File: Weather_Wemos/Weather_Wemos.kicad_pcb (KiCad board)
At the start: 2 copper layers, 62 x 85 mm, 23 parts, among them J1 Pwr In, J2 12V, J3 Rain3 Adv, J4 WIND, J5 RAIN1, J6 Rain2 Serial, J7 Exp, U1 WeMos_D1_mini, U2 L7805

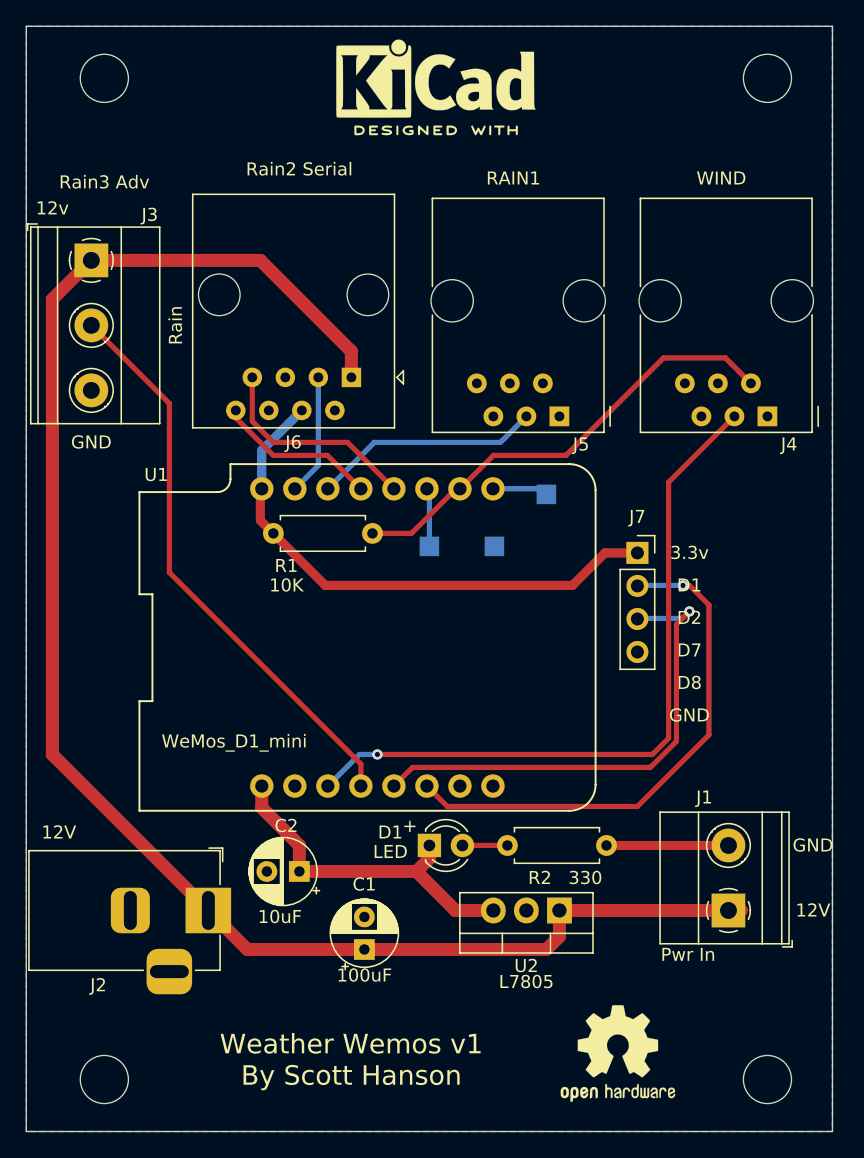
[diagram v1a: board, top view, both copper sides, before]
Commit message: upgraded to 6, changed pinout
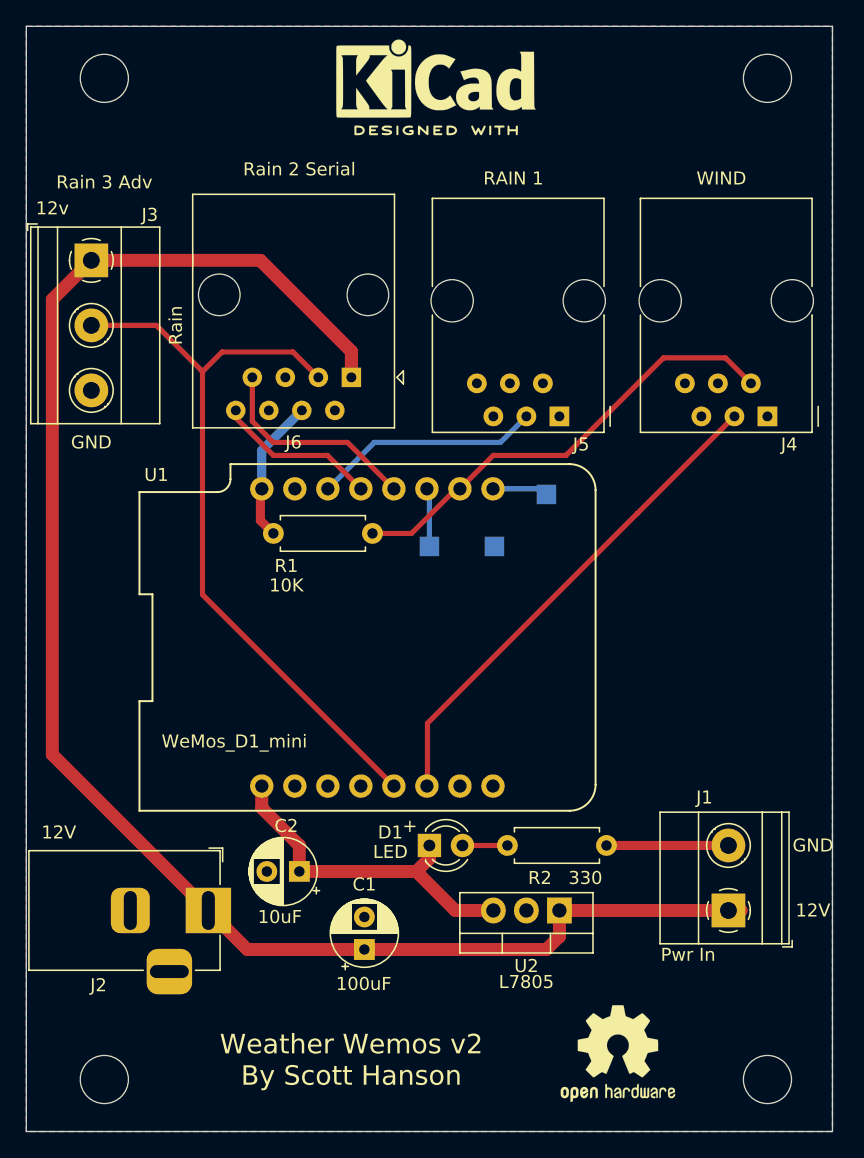
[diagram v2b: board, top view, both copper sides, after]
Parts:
- removed J7: Exp, Connector_PinSocket_2.54mm:PinSocket_1x04_P2.54mm_Vertical
- J3: value Rain3 Adv -> Rain 3 Adv
- J5: value RAIN1 -> RAIN 1
- J6: value Rain2 Serial -> Rain 2 Serial
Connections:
- J3 pad 2: RAIN3 -> RAIN2
- J4 pad 1: Net-(J4-Pad1) -> unconnected-(J4-Pad1)
- J4 pad 6: Net-(J4-Pad6) -> unconnected-(J4-Pad6)
- J5 pad 1: Net-(J5-Pad1) -> unconnected-(J5-Pad1)
- J5 pad 2: Net-(J5-Pad2) -> unconnected-(J5-Pad2)
- J5 pad 5: Net-(J5-Pad5) -> unconnected-(J5-Pad5)
- J5 pad 6: Net-(J5-Pad6) -> unconnected-(J5-Pad6)
- U1 pad 11: WSPEED -> unconnected-(U1-Pad11)
- U1 pad 12: RAIN3 -> unconnected-(U1-Pad12)
- U1 pad 13: D2 -> RAIN2
- U1 pad 14: D1 -> WSPEED
- U1 pad 15: Net-(U1-Pad15) -> unconnected-(U1-Pad15)
- U1 pad 16: Net-(U1-Pad16) -> unconnected-(U1-Pad16)
- U1 pad 7: RAIN2 -> unconnected-(U1-Pad7)
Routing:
- net RAIN2: track 9.75 -> 58.3 mm
- net RAIN3: track 44.0 -> 0.00 mm
- net D1: track 40.8 -> 0.00 mm, vias 1 -> 0
- net D2: track 37.8 -> 0.00 mm, vias 1 -> 0
- net +3V3: track 41.9 -> 11.2 mm
- net WSPEED: track 54.6 -> 38.2 mm, vias 1 -> 0
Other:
- net class Default removed
- net class pwr removed
- board text added: "Weather Wemos v2 By Scott Hanson"
- board text removed: "D1"
- board text removed: "D2"
- board text removed: "D7"
- board text removed: "D8"
- board text removed: "Weather Wemos v1 By Scott Hanson"

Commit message: added temperature sensor
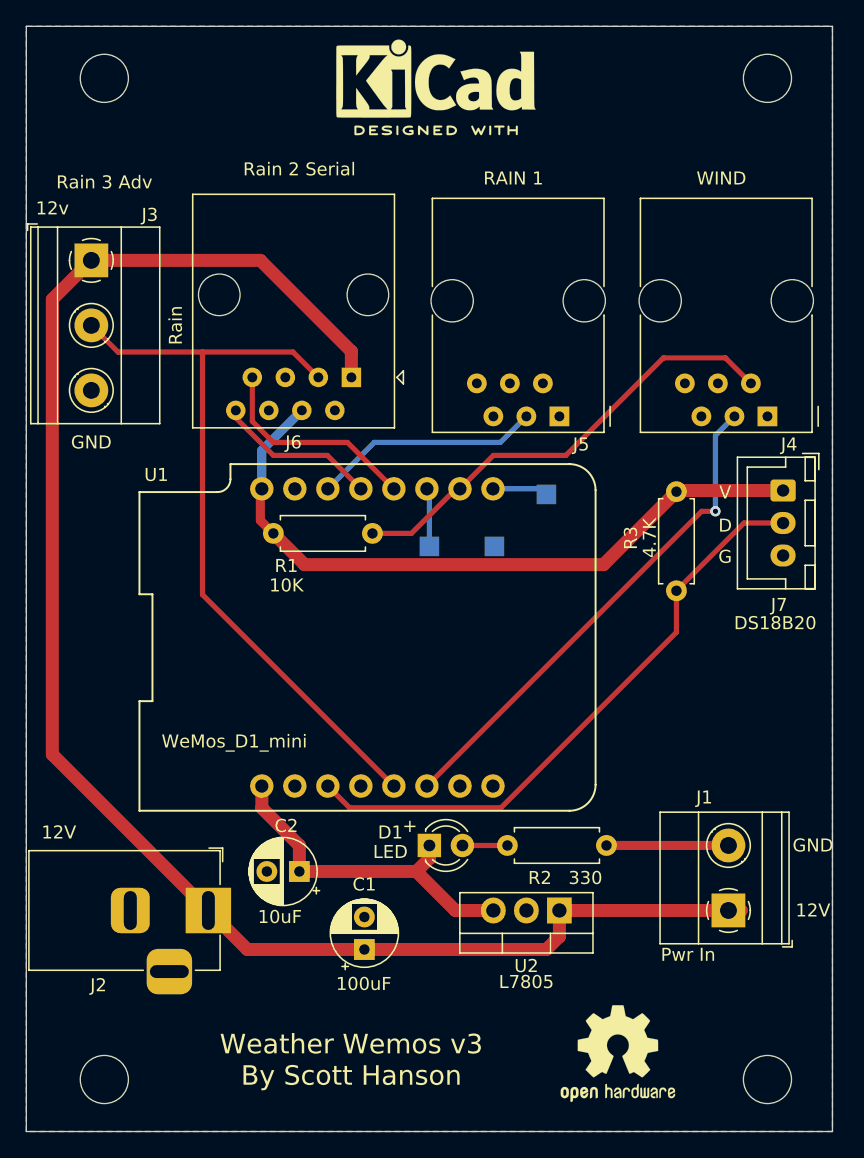
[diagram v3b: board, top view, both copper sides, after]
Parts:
- added J7: DS18B20, Connector_JST:JST_XH_B3B-XH-A_1x03_P2.50mm_Vertical, F.Cu at (177.2, 94.7)
- added R3: 4.7K, Resistor_THT:R_Axial_DIN0207_L6.3mm_D2.5mm_P7.62mm_Horizontal, F.Cu at (169.0, 102.4)
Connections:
- U1 pad 11: unconnected-(U1-Pad11) -> Net-(J7-Pin_2)
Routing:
- net Net-(J7-Pin_2): track 0.00 -> 46.6 mm
- net +3V3: track 11.2 -> 53.8 mm
- net WSPEED: track 38.2 -> 38.8 mm, vias 0 -> 1
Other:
- board text added: "${TITLE} ${REVISION} By ${COMPANY}"
- board text added: "D"
- board text added: "G"
- board text added: "V"
- board text removed: "Weather Wemos v2 By Scott Hanson"

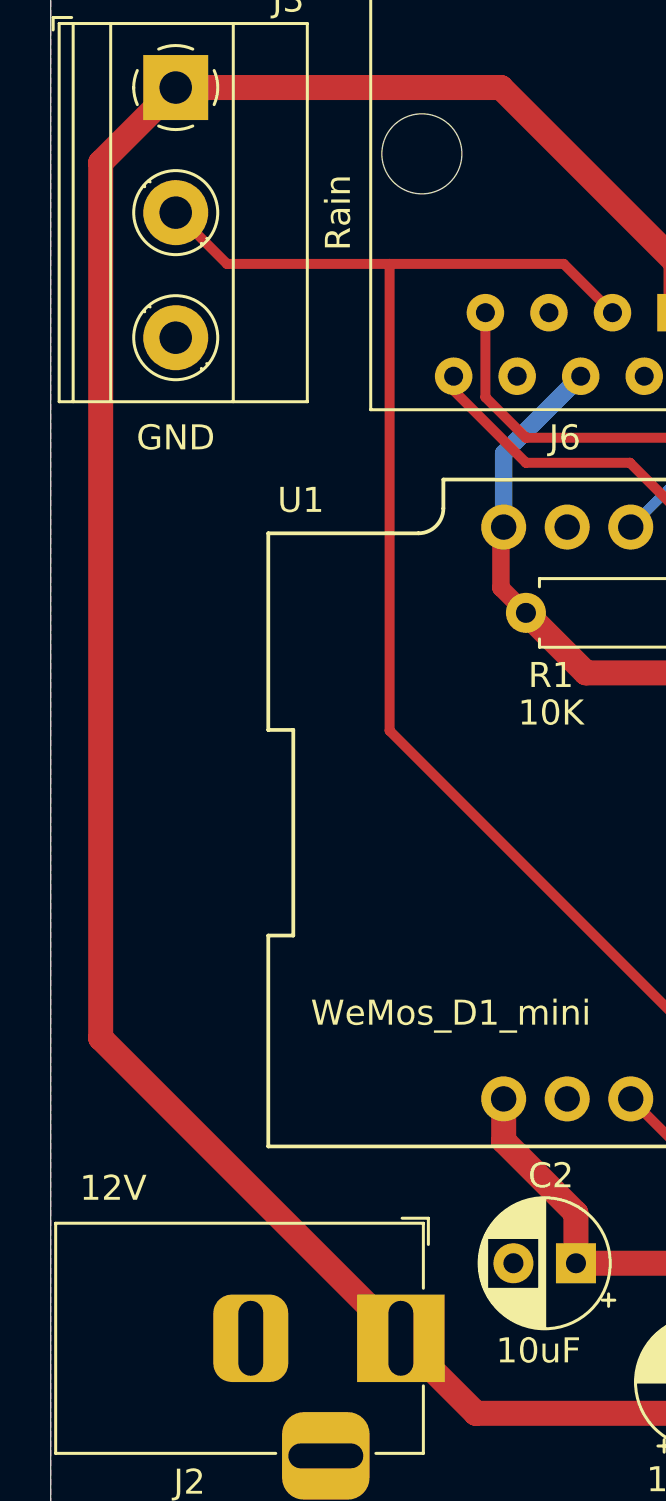
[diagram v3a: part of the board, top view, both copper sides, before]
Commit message: add plug in 3 to 4 adapter
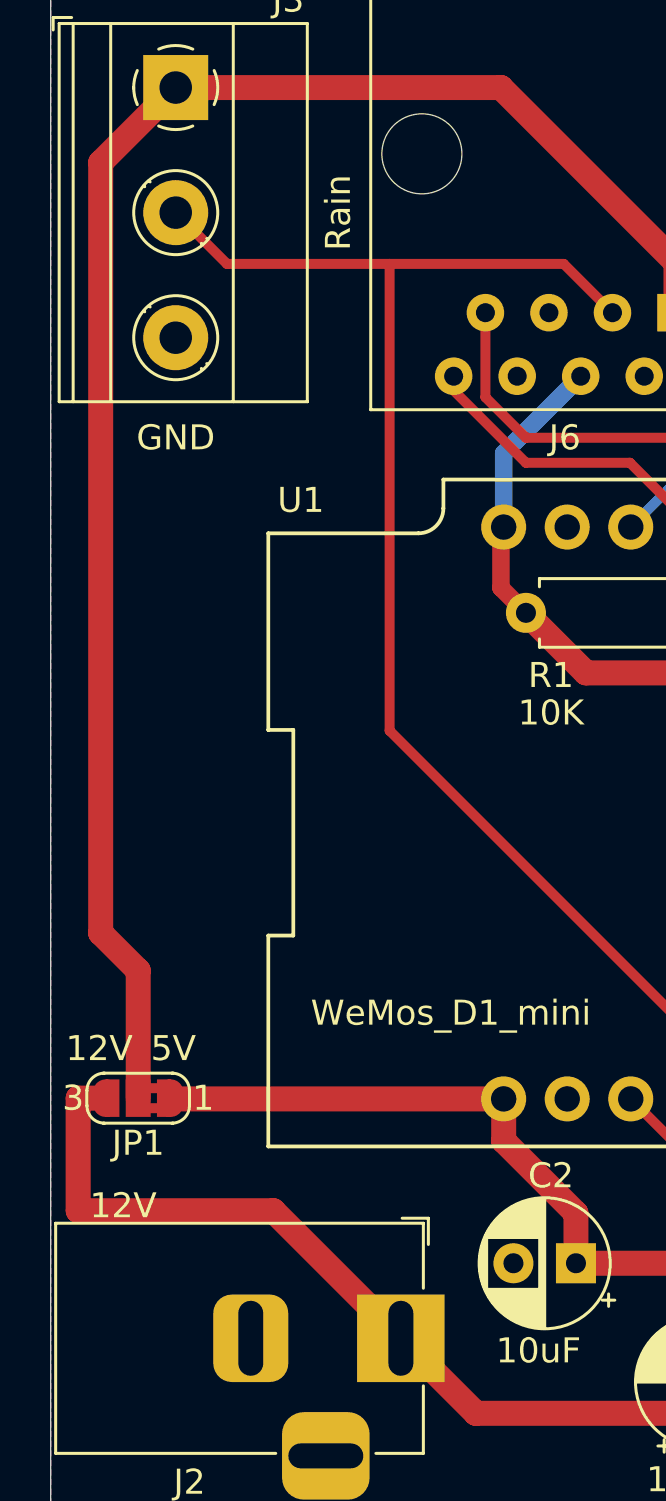
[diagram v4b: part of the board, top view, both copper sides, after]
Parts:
- added JP1: Rain_PWR_Jumper, Jumper:SolderJumper-3_P1.3mm_Bridged2Bar12_RoundedPad1.0x1.5mm_NumberLabels, F.Cu at (122.5, 117.4)
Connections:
- J3 pad 1: +12V -> RAIN_PWR
- J6 pad 1: +12V -> RAIN_PWR
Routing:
- net RAIN_PWR: track 0.00 -> 67.2 mm
- net +12V: track 125.8 -> 65.3 mm
- net +5V: track 26.3 -> 39.7 mm
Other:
- board text added: "5V"
